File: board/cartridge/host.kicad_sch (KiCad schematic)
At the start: 13 parts, among them P1 Card Edge, U4 TXS0108E, U5 74LVC245, U6 74LVT14, U7 74LVC541, U8 74LVC541, U9 PCM5100

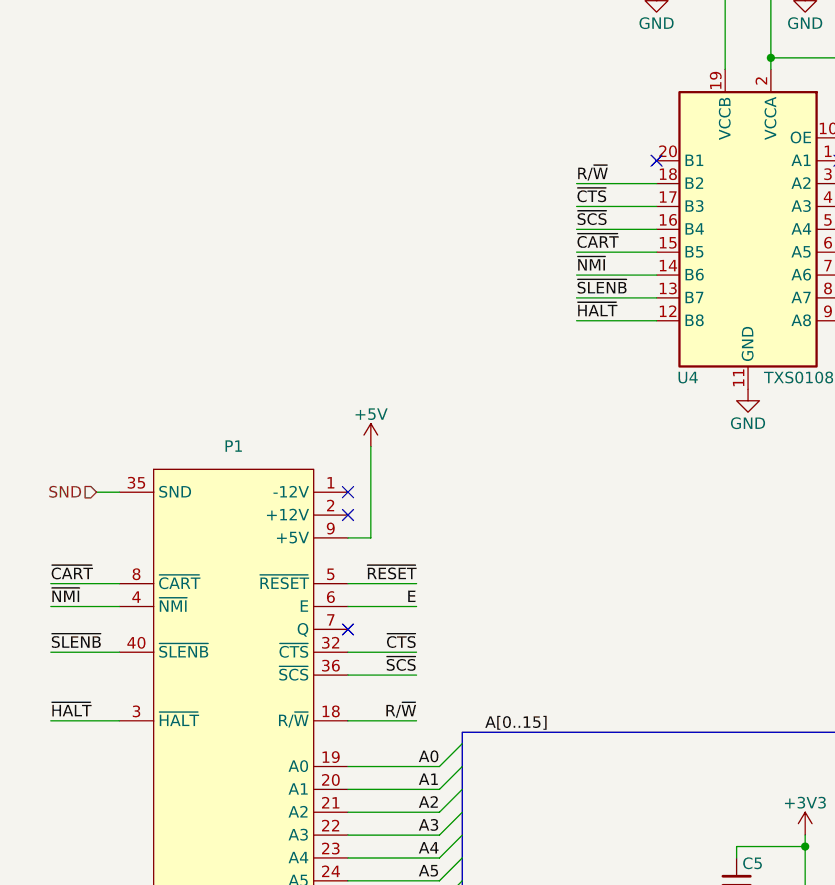
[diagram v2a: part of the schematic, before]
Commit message: Attach control bus to MCU.
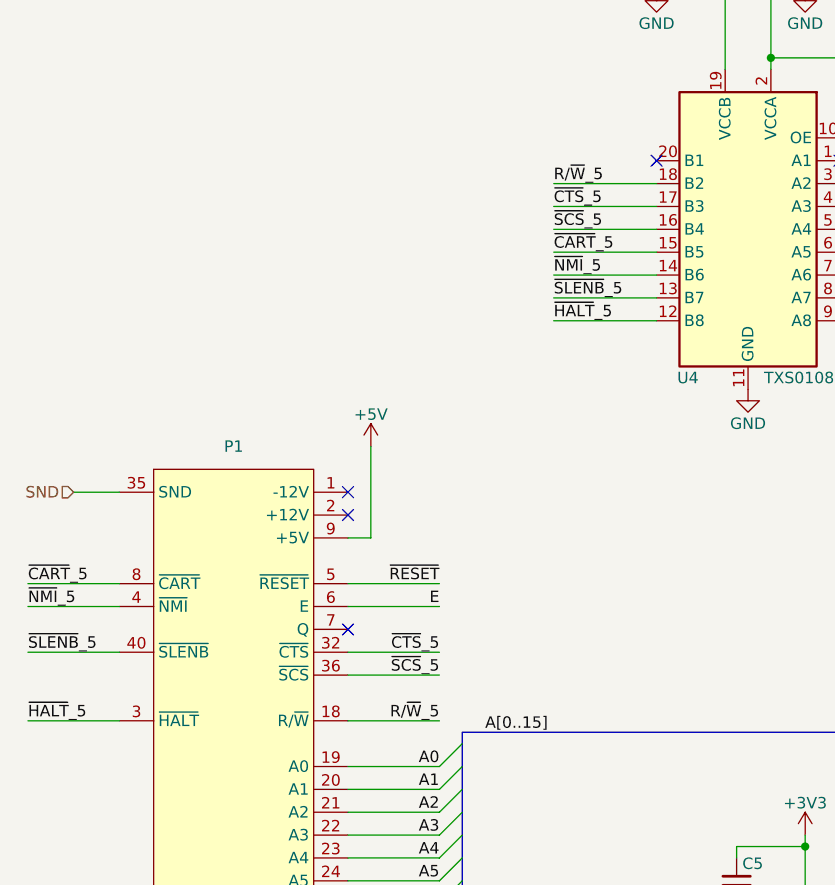
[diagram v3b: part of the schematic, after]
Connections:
- net R/~{W}: no longer P1.18 (R/~{W}), U4.18 (B2)
- net ~{CART}: no longer P1.8 (~{CART}), U4.15 (B5)
- net ~{CTS}: no longer P1.32 (~{CTS}), U4.17 (B3)
- net ~{HALT}: no longer P1.3 (~{HALT}), U4.12 (B8)
- net ~{NMI}: no longer P1.4 (~{NMI}), U4.14 (B6)
- net ~{SCS}: no longer P1.36 (~{SCS}), U4.16 (B4)
- net ~{SLENB}: no longer P1.40 (~{SLENB}), U4.13 (B7)
- new net R/~{W}_5: P1.18 (R/~{W}), U4.18 (B2)
- new net ~{CART}_5: P1.8 (~{CART}), U4.15 (B5)
- new net ~{CTS}_5: P1.32 (~{CTS}), U4.17 (B3)
- new net ~{HALT}_5: P1.3 (~{HALT}), U4.12 (B8)
- new net ~{NMI}_5: P1.4 (~{NMI}), U4.14 (B6)
- new net ~{SCS}_5: P1.36 (~{SCS}), U4.16 (B4)
- new net ~{SLENB}_5: P1.40 (~{SLENB}), U4.13 (B7)
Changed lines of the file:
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@@
 	(wire
 		(pts
-			(xy 77.47 50.8) (xy 86.36 50.8)
+			(xy 74.93 50.8) (xy 86.36 50.8)
 		)
 		(stroke
@@
 	(wire
 		(pts
-			(xy 52.07 95.25) (xy 59.69 95.25)
+			(xy 52.07 95.25) (xy 62.23 95.25)
 		)
 		(stroke
@@
 	(wire
 		(pts
-			(xy 86.36 55.88) (xy 77.47 55.88)
+			(xy 86.36 55.88) (xy 74.93 55.88)
 		)
 		(stroke
@@
 	(wire
 		(pts
-			(xy 52.07 102.87) (xy 59.69 102.87)
+			(xy 52.07 102.87) (xy 62.23 102.87)
 		)
 		(stroke
@@
 	(wire
 		(pts
-			(xy 86.36 53.34) (xy 77.47 53.34)
+			(xy 86.36 53.34) (xy 74.93 53.34)
 		)
 		(stroke
@@
 	(wire
 		(pts
-			(xy 19.05 107.95) (xy 26.67 107.95)
+			(xy 16.51 107.95) (xy 26.67 107.95)
 		)
 		(stroke
@@
 	(wire
 		(pts
-			(xy 52.07 92.71) (xy 59.69 92.71)
+			(xy 52.07 92.71) (xy 62.23 92.71)
 		)
 		(stroke
@@
 	(wire
 		(pts
-			(xy 86.36 63.5) (xy 77.47 63.5)
+			(xy 86.36 63.5) (xy 74.93 63.5)
 		)
 		(stroke
@@
 	(wire
 		(pts
-			(xy 86.36 58.42) (xy 77.47 58.42)
+			(xy 86.36 58.42) (xy 74.93 58.42)
 		)
 		(stroke
@@
 	(wire
 		(pts
-			(xy 24.13 82.55) (xy 26.67 82.55)
+			(xy 21.59 82.55) (xy 26.67 82.55)
 		)
 		(stroke
@@
 	(wire
 		(pts
-			(xy 86.36 48.26) (xy 77.47 48.26)
+			(xy 86.36 48.26) (xy 74.93 48.26)
 		)
 		(stroke
@@
 	(wire
 		(pts
-			(xy 52.07 107.95) (xy 59.69 107.95)
+			(xy 52.07 107.95) (xy 62.23 107.95)
 		)
 		(stroke
@@
 	(wire
 		(pts
-			(xy 19.05 95.25) (xy 26.67 95.25)
+			(xy 16.51 95.25) (xy 26.67 95.25)
 		)
 		(stroke
@@
 	(wire
 		(pts
-			(xy 52.07 100.33) (xy 59.69 100.33)
+			(xy 52.07 100.33) (xy 62.23 100.33)
 		)
 		(stroke
@@
 	(wire
 		(pts
-			(xy 86.36 60.96) (xy 77.47 60.96)
+			(xy 86.36 60.96) (xy 74.93 60.96)
 		)
 		(stroke
@@
 	(wire
 		(pts
-			(xy 19.05 92.71) (xy 26.67 92.71)
+			(xy 16.51 92.71) (xy 26.67 92.71)
 		)
 		(stroke
@@
 	(wire
 		(pts
-			(xy 19.05 100.33) (xy 26.67 100.33)
+			(xy 16.51 100.33) (xy 26.67 100.33)
 		)
 		(stroke
@@
 		)
 	)
-	(label "~{NMI}"
-		(at 77.47 58.42 0)
+	(label "~{NMI}_5"
+		(at 74.93 58.42 0)
 		(fields_autoplaced yes)
 		(effects
@@
 		)
 	)
-	(label "~{SCS}"
-		(at 59.69 102.87 180)
+	(label "~{SCS}_5"
+		(at 62.23 102.87 180)
 		(fields_autoplaced yes)
 		(effects
@@
 		)
 	)
-	(label "~{CART}"
-		(at 77.47 55.88 0)
+	(label "~{CART}_5"
+		(at 74.93 55.88 0)
 		(fields_autoplaced yes)
 		(effects
@@
 		)
 	)
-	(label "~{CTS}"
-		(at 77.47 50.8 0)
+	(label "~{CTS}_5"
+		(at 74.93 50.8 0)
 		(fields_autoplaced yes)
 		(effects
@@
 		)
 	)
-	(label "~{HALT}"
-		(at 77.47 63.5 0)
+	(label "~{HALT}_5"
+		(at 74.93 63.5 0)
 		(fields_autoplaced yes)
 		(effects
@@
 		)
 	)
-	(label "~{NMI}"
-		(at 19.05 95.25 0)
+	(label "~{NMI}_5"
+		(at 16.51 95.25 0)
 		(fields_autoplaced yes)
 		(effects
@@
 		)
 	)
-	(label "~{SCS}"
-		(at 77.47 53.34 0)
+	(label "~{SCS}_5"
+		(at 74.93 53.34 0)
 		(fields_autoplaced yes)
 		(effects
@@
 	)
 	(label "~{RESET}"
-		(at 59.69 92.71 180)
+		(at 62.23 92.71 180)
 		(fields_autoplaced yes)
 		(effects
@@
 		)
 	)
-	(label "~{SLENB}"
-		(at 19.05 100.33 0)
+	(label "~{SLENB}_5"
+		(at 16.51 100.33 0)
 		(fields_autoplaced yes)
 		(effects
@@
 		)
 	)
-	(label "~{SLENB}"
-		(at 77.47 60.96 0)
+	(label "~{SLENB}_5"
+		(at 74.93 60.96 0)
 		(fields_autoplaced yes)
 		(effects
@@
 		)
 	)
-	(label "~{CTS}"
-		(at 59.69 100.33 180)
+	(label "~{CTS}_5"
+		(at 62.23 100.33 180)
 		(fields_autoplaced yes)
 		(effects
@@
 		)
 	)
-	(label "R{slash}~{W}"
-		(at 59.69 107.95 180)
+	(label "R{slash}~{W}_5"
+		(at 62.23 107.95 180)
 		(fields_autoplaced yes)
 		(effects
@@
 	)
 	(label "E"
-		(at 59.69 95.25 180)
+		(at 62.23 95.25 180)
 		(fields_autoplaced yes)
 		(effects
@@
 		)
 	)
-	(label "~{CART}"
-		(at 19.05 92.71 0)
+	(label "~{CART}_5"
+		(at 16.51 92.71 0)
 		(fields_autoplaced yes)
 		(effects
@@
 		)
 	)
-	(label "R{slash}~{W}"
-		(at 77.47 48.26 0)
+	(label "R{slash}~{W}_5"
+		(at 74.93 48.26 0)
 		(fields_autoplaced yes)
 		(effects
@@
 		)
 	)
-	(label "~{HALT}"
-		(at 19.05 107.95 0)
+	(label "~{HALT}_5"
+		(at 16.51 107.95 0)
 		(fields_autoplaced yes)
 		(effects
@@
 	(hierarchical_label "SND"
 		(shape input)
-		(at 24.13 82.55 180)
+		(at 21.59 82.55 180)
 		(fields_autoplaced yes)
 		(effects

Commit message: More bus routing.
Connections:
- net I2S_BCK: now reaches U9.13 (BCK)
- net I2S_DIN: now reaches U9.14 (DIN)
- net I2S_LRCK: now reaches U9.15 (LRCK)
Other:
- moved on the sheet: C9, U6G

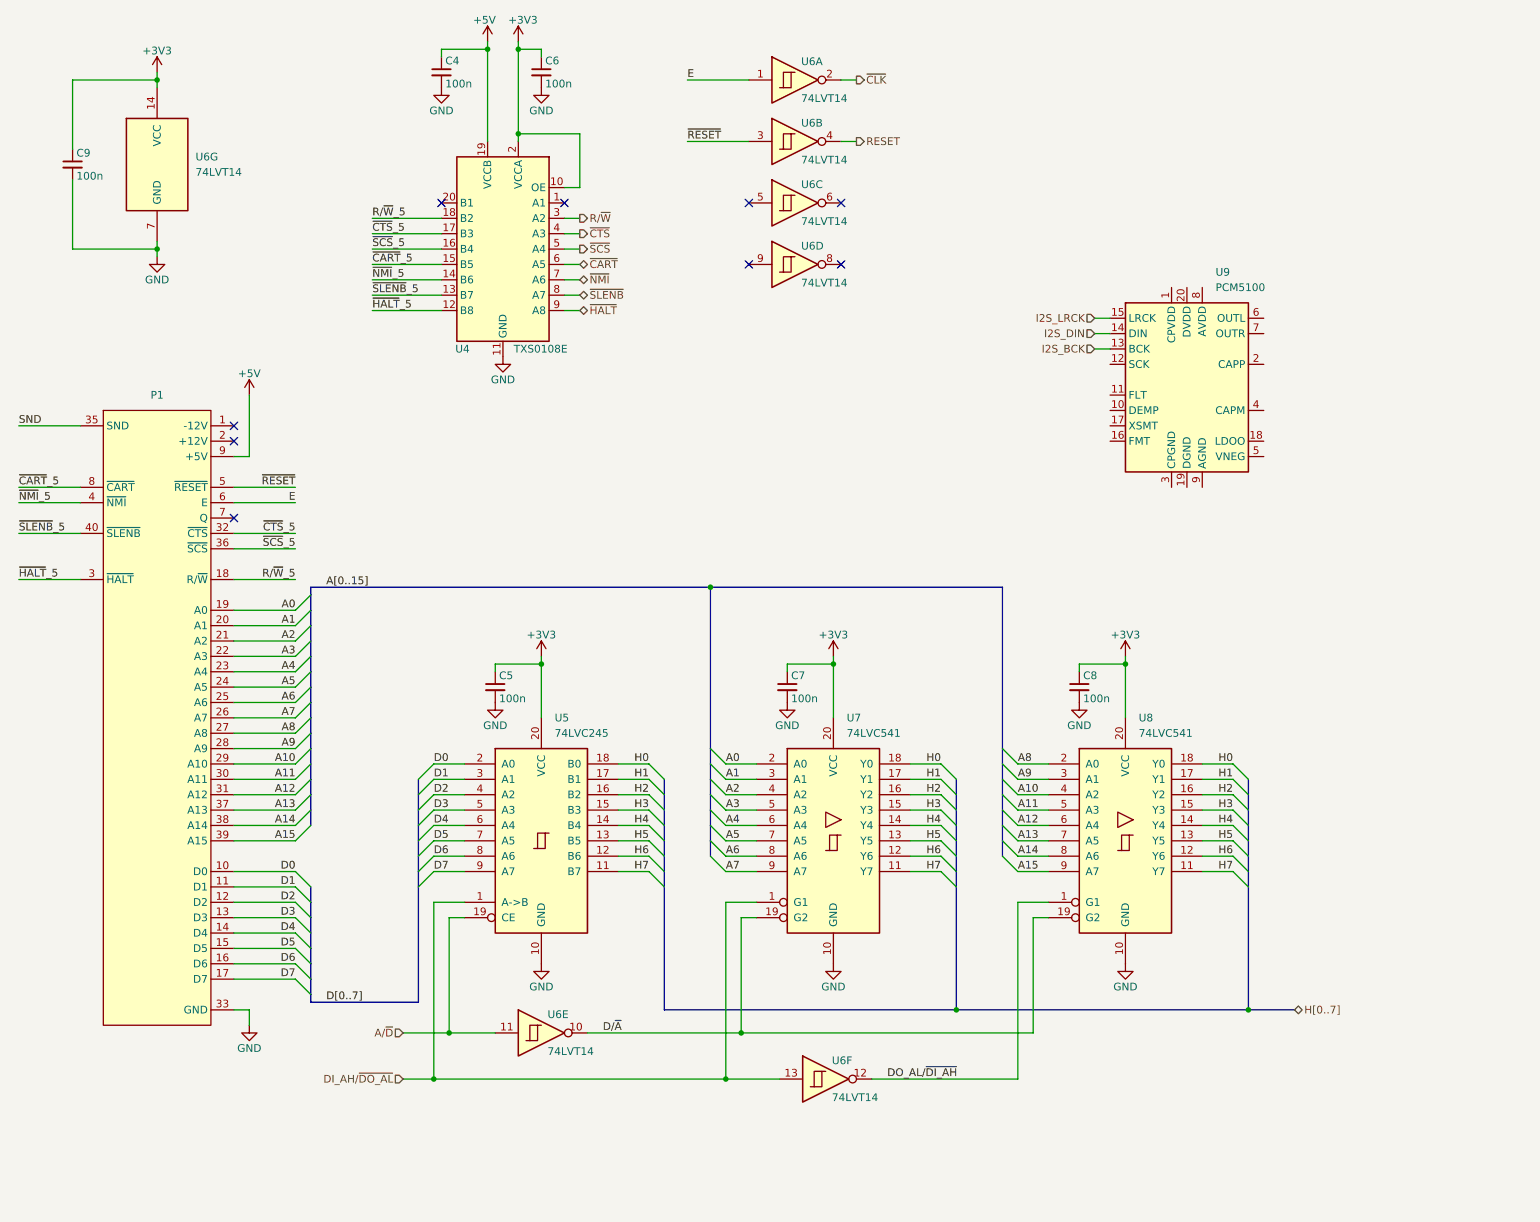
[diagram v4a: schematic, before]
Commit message: Re-route CoCo bus with all 74-245s.
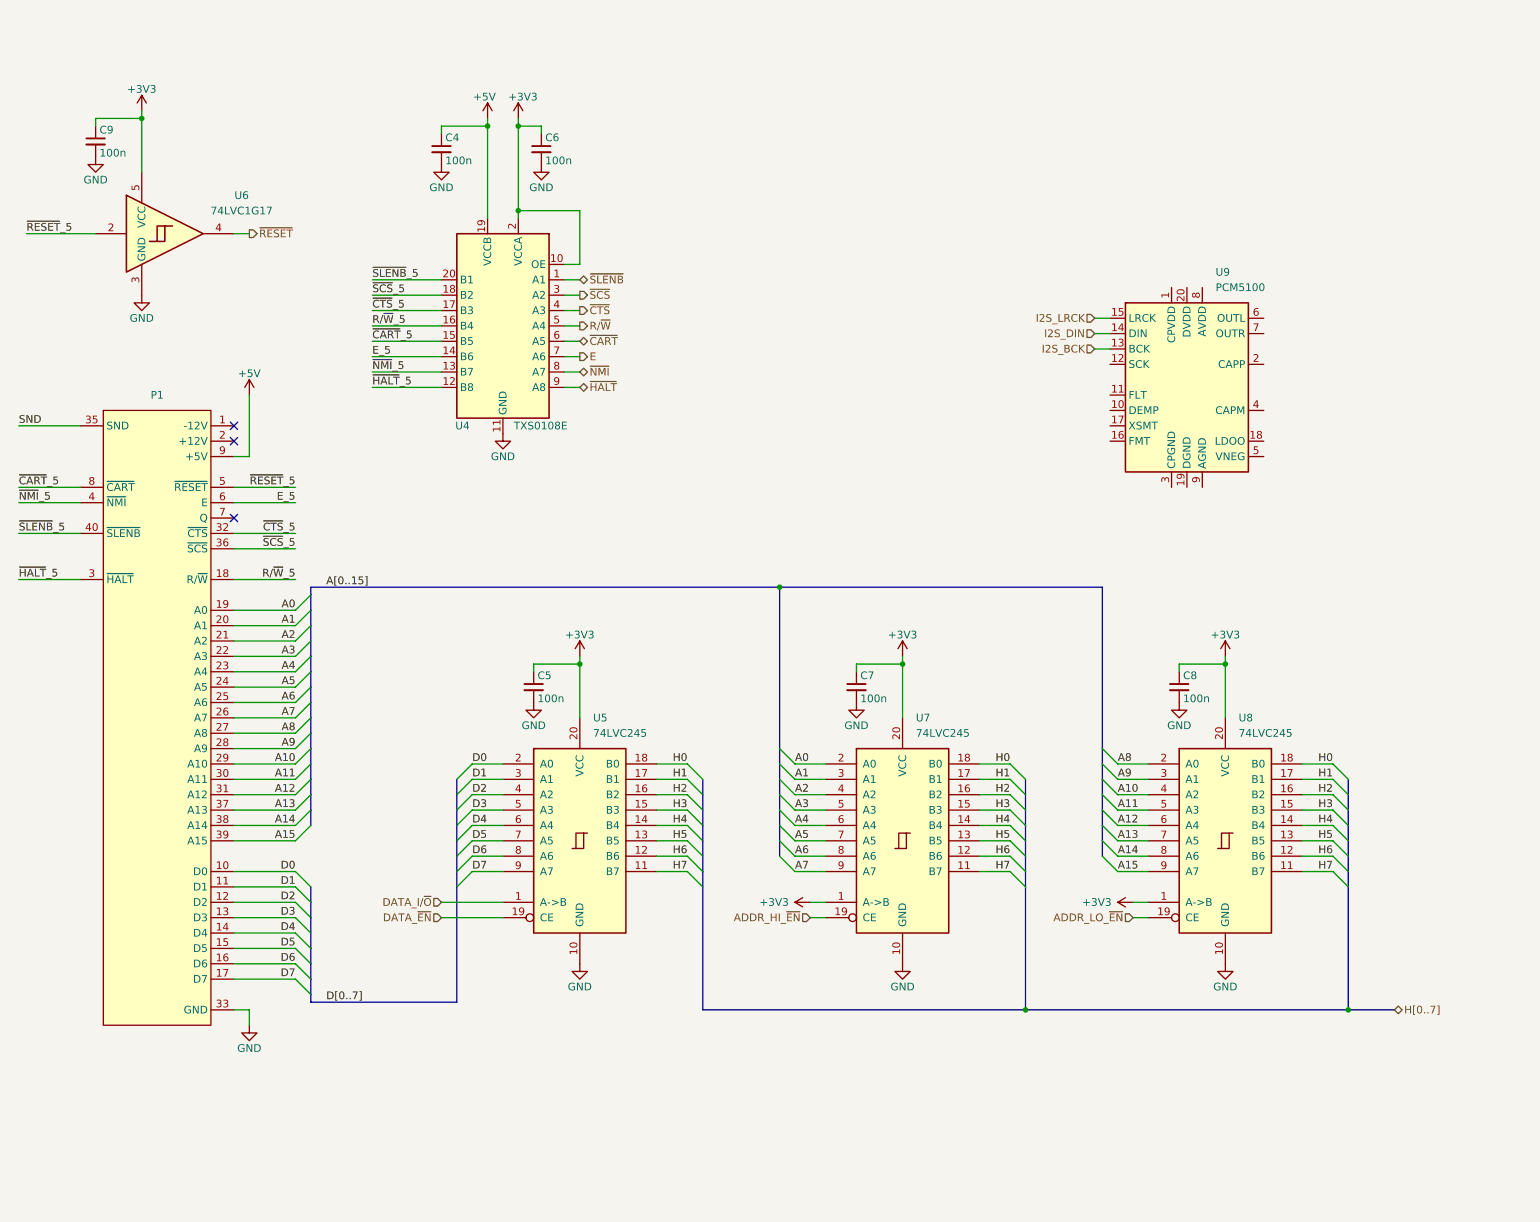
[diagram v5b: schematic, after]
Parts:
- removed U6: 74LVT14, Package_SO:TSSOP-14_4.4x5mm_P0.65mm, symbol 74xx:74HC14
- removed U7, U8: 74LVC541, Package_SO:TSSOP-20_4.4x6.5mm_P0.65mm, symbol 74xx:74LS541
- added U6: 74LVC1G17, Package_TO_SOT_SMD:SOT-353_SC-70-5, symbol 74xGxx:74LVC1G17
- added U7, U8: 74LVC245, Package_SO:TSSOP-20_4.4x6.5mm_P0.65mm, symbol 74xx:74LS245
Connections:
- net +3V3: now also U6.5 (VCC), U7.1 (A->B), U7.20 (VCC), U8.1 (A->B), U8.20 (VCC)
- net A0: now also U7.2 (A0)
- net A1: now also U7.3 (A1)
- net A10: now also U8.4 (A2)
- net A11: now also U8.5 (A3)
- net A12: now also U8.6 (A4)
- net A13: now also U8.7 (A5)
- net A14: now also U8.8 (A6)
- net A15: now also U8.9 (A7)
- net A2: now also U7.4 (A2)
- net A3: now also U7.5 (A3)
- net A4: now also U7.6 (A4)
- net A5: now also U7.7 (A5)
- net A6: now also U7.8 (A6)
- net A7: now also U7.9 (A7)
- net A8: now also U8.2 (A0)
- net A9: now also U8.3 (A1)
- net E: now also U4.7 (A6); no longer P1.6 (E)
- net GND: now also U6.3 (GND), U7.10 (GND), U8.10 (GND)
- net H0: now also U7.18 (B0), U8.18 (B0)
- net H1: now also U7.17 (B1), U8.17 (B1)
- net H2: now also U7.16 (B2), U8.16 (B2)
- net H3: now also U7.15 (B3), U8.15 (B3)
- net H4: now also U7.14 (B4), U8.14 (B4)
- net H5: now also U7.13 (B5), U8.13 (B5)
- net H6: now also U7.12 (B6), U8.12 (B6)
- net H7: now also U7.11 (B7), U8.11 (B7)
- net R/~{W}: now also U4.5 (A4); no longer U4.3 (A2)
- net R/~{W}_5: now also U4.16 (B4); no longer U4.18 (B2)
- net ~{NMI}: now also U4.8 (A7); no longer U4.7 (A6)
- net ~{NMI}_5: now also U4.13 (B7); no longer U4.14 (B6)
- net ~{RESET}: now also U6.4; no longer P1.5 (~{RESET})
- net ~{SCS}: now also U4.3 (A2); no longer U4.5 (A4)
- net ~{SCS}_5: now also U4.18 (B2); no longer U4.16 (B4)
- net ~{SLENB}: now also U4.1 (A1); no longer U4.8 (A7)
- net ~{SLENB}_5: now also U4.20 (B1); no longer U4.13 (B7)
- net A/~{D} renamed DATA_~{EN}
- net DI_AH/~{DO_AL} renamed DATA_I/~{O}
- new net ADDR_HI_~{EN}: U7.19 (CE)
- new net ADDR_LO_~{EN}: U8.19 (CE)
- new net E_5: P1.6 (E), U4.14 (B6)
- new net ~{RESET}_5: P1.5 (~{RESET}), U6.2
- no-connect marks 9 -> 3
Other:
- company: © 2023 Sam Hanes, licensed CERN-OHL-W v2 -> © 2023-2024 Sam Hanes, licensed CERN-OHL-W v2
- moved on the sheet: C4, C5, C6, C7, C8, U4, U5

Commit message: Finish USB power management.
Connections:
- net +5V renamed +5V_HOST
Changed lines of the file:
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@@
-	)
-	(symbol
-		(lib_id "power:+5V")
-		(at 93.98 31.75 0)
-		(mirror y)
-		(unit 1)
-		(exclude_from_sim no)
-		(in_bom yes)
-		(on_board yes)
-		(dnp no)
-		(property "Reference" "#PWR022"
-			(at 93.98 35.56 0)
-			(effects
-				(font
-					(size 1.27 1.27)
-				)
-				(hide yes)
-			)
-		)
-		(property "Value" "+5V"
-			(at 93.472 28.194 0)
-			(effects
-				(font
-					(size 1.27 1.27)
-				)
-			)
-		)
-		(property "Footprint" ""
-			(at 93.98 31.75 0)
-			(effects
-				(font
-					(size 1.27 1.27)
-				)
-				(hide yes)
-			)
-		)
-		(property "Datasheet" ""
-			(at 93.98 31.75 0)
-			(effects
-				(font
-					(size 1.27 1.27)
-				)
-				(hide yes)
-			)
-		)
-		(property "Description" "Power symbol creates a global label with name \"+5V\""
-			(at 93.98 31.75 0)
-			(effects
-				(font
-					(size 1.27 1.27)
-				)
-				(hide yes)
-			)
-		)
-		(pin "1"
-		)
-		(instances
-			(project "cartridge"
-				(path "/b6472d2e-e93c-4ee2-a887-2e70fff347c6/c8484109-b338-40e2-9818-5e104bae91b8"
-					(reference "#PWR022")
-					(unit 1)
-				)
-			)
-		)
 	)
 	(symbol
@@
 	)
 	(symbol
+		(lib_id "0Project:+5V_HOST")
+		(at 93.98 31.75 0)
+		(unit 1)
+		(exclude_from_sim no)
+		(in_bom yes)
+		(on_board yes)
+		(dnp no)
+		(property "Reference" "#PWR022"
+			(at 93.98 35.56 0)
+			(effects
+				(font
+					(size 1.27 1.27)
+				)
+				(hide yes)
+			)
+		)
+		(property "Value" "+5V_HOST"
+			(at 95.25 28.194 0)
+			(effects
+				(font
+					(size 1.27 1.27)
+				)
+				(justify right)
+			)
+		)
+		(property "Footprint" ""
+			(at 93.98 31.75 0)
+			(effects
+				(font
+					(size 1.27 1.27)
+				)
+				(hide yes)
+			)
+		)
+		(property "Datasheet" ""
+			(at 93.98 31.75 0)
+			(effects
+				(font
+					(size 1.27 1.27)
+				)
+				(hide yes)
+			)
+		)
+		(property "Description" "Power symbol creates a global label with name \"+5V\""
+			(at 93.98 31.75 0)
+			(effects
+				(font
+					(size 1.27 1.27)
+				)
+				(hide yes)
+			)
+		)
+		(pin "1"
+		)
+		(instances
+			(project "cartridge"
+				(path "/b6472d2e-e93c-4ee2-a887-2e70fff347c6/c8484109-b338-40e2-9818-5e104bae91b8"
+					(reference "#PWR022")
+					(unit 1)
+				)
+			)
+		)
+	)
+	(symbol
 		(lib_id "power:+3V3")
 		(at 109.22 120.65 0)
@@
 	)
 	(symbol
-		(lib_id "power:+5V")
-		(at 54.61 77.47 0)
-		(unit 1)
-		(exclude_from_sim no)
-		(in_bom yes)
-		(on_board yes)
-		(dnp no)
-		(property "Reference" "#PWR019"
-			(at 54.61 81.28 0)
-			(effects
-				(font
-					(size 1.27 1.27)
-				)
-				(hide yes)
-			)
-		)
-		(property "Value" "+5V"
-			(at 54.61 73.914 0)
-			(effects
-				(font
-					(size 1.27 1.27)
-				)
-			)
-		)
-		(property "Footprint" ""
-			(at 54.61 77.47 0)
-			(effects
-				(font
-					(size 1.27 1.27)
-				)
-				(hide yes)
-			)
-		)
-		(property "Datasheet" ""
-			(at 54.61 77.47 0)
-			(effects
-				(font
-					(size 1.27 1.27)
-				)
-				(hide yes)
-			)
-		)
-		(property "Description" "Power symbol creates a global label with name \"+5V\""
-			(at 54.61 77.47 0)
-			(effects
-				(font
-					(size 1.27 1.27)
-				)
-				(hide yes)
-			)
-		)
-		(pin "1"
-		)
-		(instances
-			(project "cartridge"
-				(path "/b6472d2e-e93c-4ee2-a887-2e70fff347c6/c8484109-b338-40e2-9818-5e104bae91b8"
-					(reference "#PWR019")
-					(unit 1)
-				)
-			)
-		)
-	)
-	(symbol
 		(lib_id "power:+3V3")
 		(at 200.66 161.29 90)
@@
 	)
 	(symbol
+		(lib_id "0Project:+5V_HOST")
+		(at 54.61 77.47 0)
+		(unit 1)
+		(exclude_from_sim no)
+		(in_bom yes)
+		(on_board yes)
+		(dnp no)
+		(property "Reference" "#PWR019"
+			(at 54.61 81.28 0)
+			(effects
+				(font
+					(size 1.27 1.27)
+				)
+				(hide yes)
+			)
+		)
+		(property "Value" "+5V_HOST"
+			(at 54.61 73.914 0)
+			(effects
+				(font
+					(size 1.27 1.27)
+				)
+			)
+		)
+		(property "Footprint" ""
+			(at 54.61 77.47 0)
+			(effects
+				(font
+					(size 1.27 1.27)
+				)
+				(hide yes)
+			)
+		)
+		(property "Datasheet" ""
+			(at 54.61 77.47 0)
+			(effects
+				(font
+					(size 1.27 1.27)
+				)
+				(hide yes)
+			)
+		)
+		(property "Description" "Power symbol creates a global label with name \"+5V\""
+			(at 54.61 77.47 0)
+			(effects
+				(font
+					(size 1.27 1.27)
+				)
+				(hide yes)
+			)
+		)
+		(pin "1"
+		)
+		(instances
+			(project ""
+				(path "/b6472d2e-e93c-4ee2-a887-2e70fff347c6/c8484109-b338-40e2-9818-5e104bae91b8"
+					(reference "#PWR019")
+					(unit 1)
+				)
+			)
+		)
+	)
+	(symbol
 		(lib_id "Device:C_Small")
 		(at 101.6 125.73 0)
@@
 		)
 		(property "Value" "+3V3"
-			(at 99.822 28.194 0)
-			(effects
-				(font
-					(size 1.27 1.27)
-				)
-			)
-		)
+			(at 97.282 28.194 0)
+			(effects
+				(font
+					(size 1.27 1.27)
+				)
+				(justify right)
+			)
+		)
